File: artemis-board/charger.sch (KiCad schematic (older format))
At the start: 23 parts, among them J10 External NTC, J2 Thermistor, Q2 2N7002, SW2 DNP, U3 LC709203FQH, U4 TP4056, U8 XC6206P332MR

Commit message: added part number for button
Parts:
- SW2: LCSC (none) -> C231329
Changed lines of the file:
@@
 F 2 "Button_Switch_SMD:SW_Push_SPST_NO_Alps_SKRK" H 3200 4500 50  0001 C CNN
 F 3 "~" H 3200 4500 50  0001 C CNN
+F 4 "C231329" H 3200 4500 50  0001 C CNN "LCSC"
 	1    3200 4500
 	1    0    0    -1

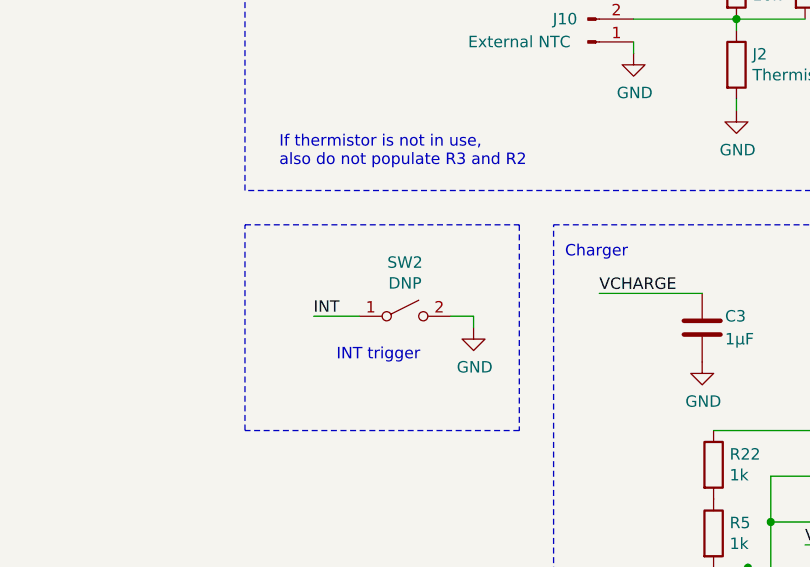
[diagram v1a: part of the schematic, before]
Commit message: changed switch value
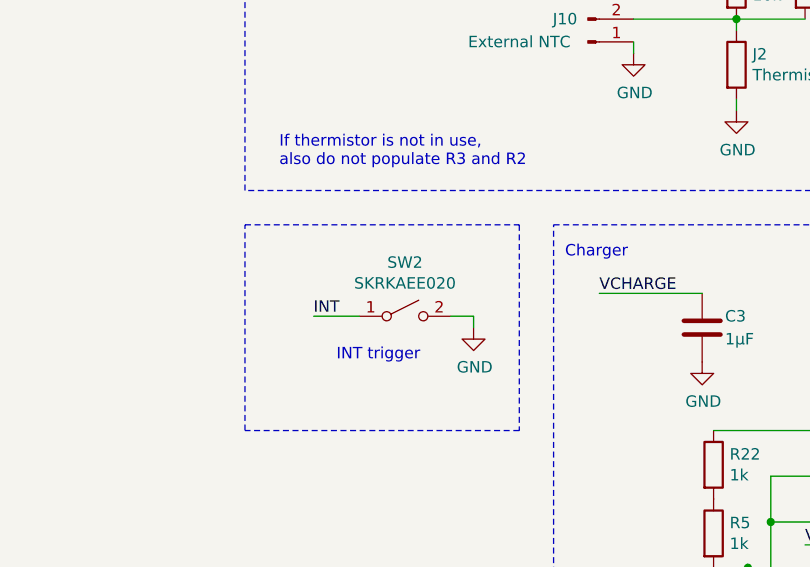
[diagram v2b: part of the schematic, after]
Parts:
- SW2: value DNP -> SKRKAEE020
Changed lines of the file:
@@
 AR Path="/5F639F48/601AEE0F" Ref="SW2"  Part="1"
 F 0 "SW2" H 3200 4735 50  0000 C CNN
-F 1 "DNP" H 3200 4644 50  0000 C CNN
+F 1 "SKRKAEE020" H 3200 4644 50  0000 C CNN
 F 2 "Button_Switch_SMD:SW_Push_SPST_NO_Alps_SKRK" H 3200 4500 50  0001 C CNN
 F 3 "~" H 3200 4500 50  0001 C CNN

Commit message: applied changes to board
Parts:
- removed R5: 1k, Resistor_SMD:R_0603_1608Metric_Pad1.05x0.95mm_HandSolder, symbol Device:R
- R22: value 1k -> 2.4k; LCSC C21190 -> C22940
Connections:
- net GND: now also R22.2
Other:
- moved on the sheet: R22
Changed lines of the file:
@@
 $Comp
 L Device:R R?
-U 1 1 5FD8F02D
+U 1 1 5FD924F7
 P 4550 5450
-AR Path="/5F639CFE/5FD8F02D" Ref="R?"  Part="1"
-AR Path="/5F639F48/5FD8F02D" Ref="R5"  Part="1"
-F 0 "R5" H 4620 5496 50  0000 L CNN
-F 1 "1k" H 4620 5405 50  0000 L CNN
+AR Path="/5F639CFE/5FD924F7" Ref="R?"  Part="1"
+AR Path="/5F639F48/5FD924F7" Ref="R22"  Part="1"
+F 0 "R22" H 4620 5496 50  0000 L CNN
+F 1 "2.4k" H 4620 5405 50  0000 L CNN
 F 2 "Resistor_SMD:R_0603_1608Metric_Pad1.05x0.95mm_HandSolder" V 4480 5450 50  0001 C CNN
 F 3 "~" H 4550 5450 50  0001 C CNN
-F 4 "C21190" H 4550 5450 50  0001 C CNN "LCSC"
+F 4 "C22940" H 4550 5450 50  0001 C CNN "LCSC"
 	1    4550 5450
 	1    0    0    -1
 $EndComp
-$Comp
-L Device:R R?
-U 1 1 5FD924F7
-P 4550 5150
-AR Path="/5F639CFE/5FD924F7" Ref="R?"  Part="1"
-AR Path="/5F639F48/5FD924F7" Ref="R22"  Part="1"
-F 0 "R22" H 4620 5196 50  0000 L CNN
-F 1 "1k" H 4620 5105 50  0000 L CNN
-F 2 "Resistor_SMD:R_0603_1608Metric_Pad1.05x0.95mm_HandSolder" V 4480 5150 50  0001 C CNN
-F 3 "~" H 4550 5150 50  0001 C CNN
-F 4 "C21190" H 4550 5150 50  0001 C CNN "LCSC"
-	1    4550 5150
-	1    0    0    -1
-$EndComp
-Wire Wire Line
-	5300 5300 5250 5300
-Wire Wire Line
-	5250 5300 5250 5000
-Wire Wire Line
-	5250 5000 4550 5000
 $Comp
 L Device:D_Schottky D?
@@
 Text Label 1550 1250 0    50   ~ 0
 3v3_I2C
+Wire Wire Line
+	4550 5300 5300 5300
 $EndSCHEMATC

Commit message: swapped switch for cheaper alps one
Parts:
- SW2: LCSC C231329 -> C115357
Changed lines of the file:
@@
 F 2 "Button_Switch_SMD:SW_Push_SPST_NO_Alps_SKRK" H 3200 4500 50  0001 C CNN
 F 3 "~" H 3200 4500 50  0001 C CNN
-F 4 "C231329" H 3200 4500 50  0001 C CNN "LCSC"
+F 4 "C115357" H 3200 4500 50  0001 C CNN "LCSC"
 	1    3200 4500
 	1    0    0    -1

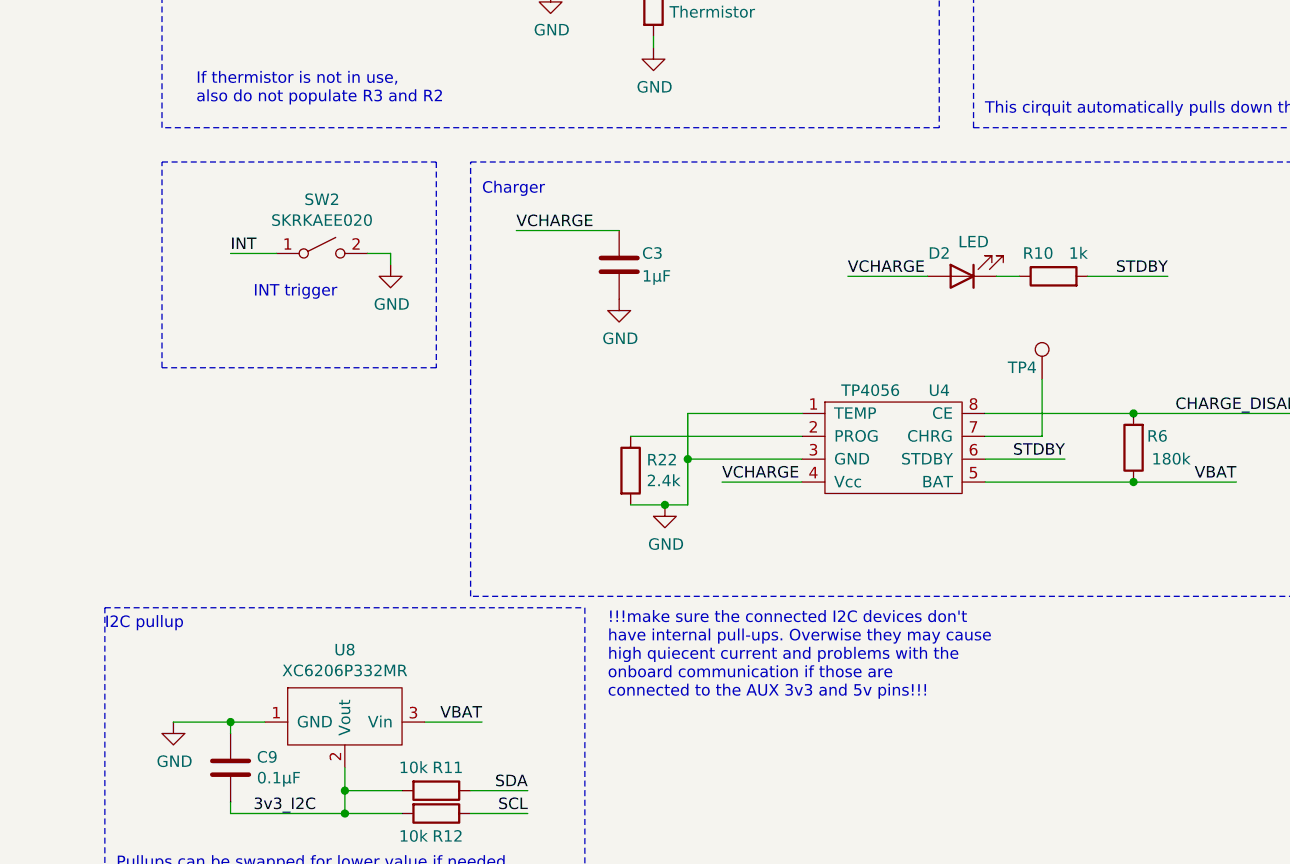
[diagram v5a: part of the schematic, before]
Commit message: added comments and swapped polarity of Vin connector
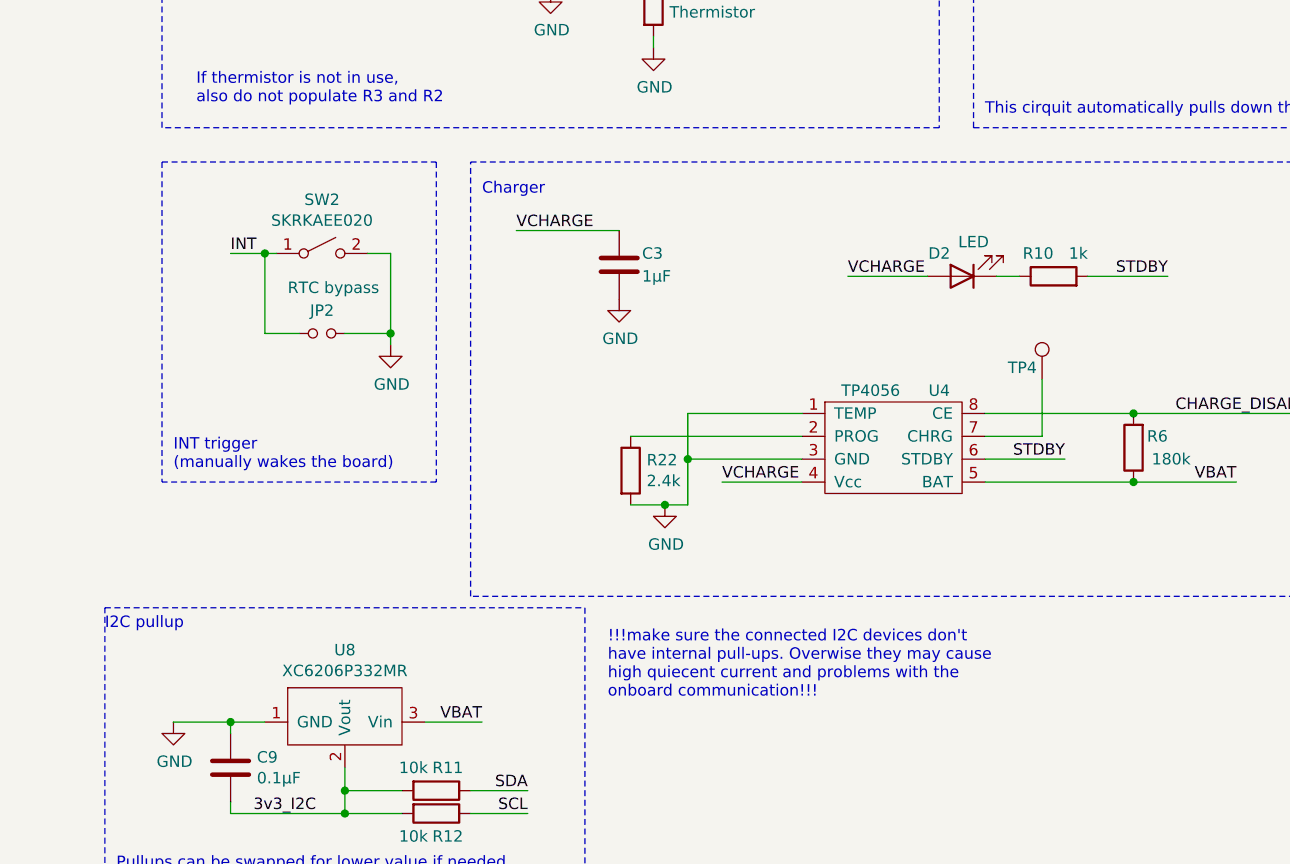
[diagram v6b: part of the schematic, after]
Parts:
- added JP2: RTC bypass, Connector_PinHeader_2.54mm:PinHeader_1x02_P2.54mm_Vertical, symbol Device:Jumper_NO_Small
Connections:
- net GND: now also JP2.1
- net INT: now also JP2.2
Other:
- note added: "!!!make sure the connected I2C devices don't\nhave internal pull-ups. Overwise they may cause\nhigh quiecent current and problems with the\nonboard communication!!!"
- note added: "INT trigger\n(manually wakes the board)"
- note removed: "!!!make sure the connected I2C devices don't\nhave internal pull-ups. Overwise they may cause\nhigh quiecent current and problems with the\nonboard communication if those are\nconnected to the AUX 3v3 and 5v pins!!!"
- note removed: "INT trigger"
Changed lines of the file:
@@
 L power:GND #PWR0133
 U 1 1 601AEE17
-P 3500 4550
-F 0 "#PWR0133" H 3500 4300 50  0001 C CNN
-F 1 "GND" H 3505 4377 50  0000 C CNN
-F 2 "" H 3500 4550 50  0001 C CNN
-F 3 "" H 3500 4550 50  0001 C CNN
-	1    3500 4550
+P 3500 4900
+F 0 "#PWR0133" H 3500 4650 50  0001 C CNN
+F 1 "GND" H 3505 4727 50  0000 C CNN
+F 2 "" H 3500 4900 50  0001 C CNN
+F 3 "" H 3500 4900 50  0001 C CNN
+	1    3500 4900
 	1    0    0    -1
 $EndComp
-Wire Wire Line
-	3500 4550 3500 4500
 Wire Wire Line
 	3400 4500 3500 4500
@@
 INT
 Wire Wire Line
-	3000 4500 2800 4500
-Text Notes 2900 4700 0    50   ~ 0
-INT trigger
+	3000 4500 2950 4500
+Text Notes 2550 5450 0    50   ~ 0
+INT trigger\n(manually wakes the board)
 Wire Notes Line
 	2500 4100 3700 4100
 Wire Notes Line
-	3700 4100 3700 5000
-Wire Notes Line
-	3700 5000 2500 5000
-Wire Notes Line
-	2500 5000 2500 4100
+	3700 5500 2500 5500
 Wire Notes Line
 	2350 600  2350 2100
@@
 Pullups can be swapped for lower value if needed
 Text Notes 4450 6450 0    50   ~ 0
-!!!make sure the connected I2C devices don't\nhave internal pull-ups. Overwise they may cause\nhigh quiecent current and problems with the\nonboard communication if those are\nconnected to the AUX 3v3 and 5v pins!!!
+!!!make sure the connected I2C devices don't\nhave internal pull-ups. Overwise they may cause\nhigh quiecent current and problems with the\nonboard communication!!!
 Text Label 2900 6950 0    50   ~ 0
 3v3_I2C
@@
 Wire Wire Line
 	4550 5300 5300 5300
+$Comp
+L Device:Jumper_NO_Small JP?
+U 1 1 60B74E13
+P 3200 4850
+AR Path="/5F63A0E9/60B74E13" Ref="JP?"  Part="1"
+AR Path="/5F639F48/60B74E13" Ref="JP2"  Part="1"
+F 0 "JP2" H 3200 4750 50  0000 C CNN
+F 1 "RTC bypass" H 3150 4650 50  0000 C CNN
+F 2 "Connector_PinHeader_2.54mm:PinHeader_1x02_P2.54mm_Vertical" H 3200 4850 50  0001 C CNN
+F 3 "~" H 3200 4850 50  0001 C CNN
+	1    3200 4850
+	-1   0    0    1
+$EndComp
+Wire Notes Line
+	3700 4100 3700 5500
+Wire Wire Line
+	3500 4850 3500 4900
+Wire Wire Line
+	3300 4850 3500 4850
+Wire Wire Line
+	3500 4500 3500 4850
+Connection ~ 3500 4850
+Wire Wire Line
+	3100 4850 2950 4850
+Wire Wire Line
+	2950 4850 2950 4500
+Connection ~ 2950 4500
+Wire Wire Line
+	2950 4500 2800 4500
+Wire Notes Line
+	2500 4100 2500 5500
 $EndSCHEMATC

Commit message: added 1µ cap close to 3v3 I2C regulator
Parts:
- added C27: 1µF, Capacitor_SMD:C_0603_1608Metric_Pad1.08x0.95mm_HandSolder, symbol Device:C
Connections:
- net GND: now also C27.2
- net VBAT: now also C27.1
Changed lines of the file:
@@
 SDA
 Wire Wire Line
-	2800 6550 2550 6550
+	2800 6550 2700 6550
 $Comp
 L power:GND #PWR?
@@
 Wire Notes Line
 	2500 4100 2500 5500
+$Comp
+L Device:C C27
+U 1 1 60B69250
+P 2700 6400
+F 0 "C27" H 2800 6450 50  0000 L CNN
+F 1 "1µF" H 2800 6350 50  0000 L CNN
+F 2 "Capacitor_SMD:C_0603_1608Metric_Pad1.08x0.95mm_HandSolder" H 2738 6250 50  0001 C CNN
+F 3 "~" H 2700 6400 50  0001 C CNN
+F 4 "C15849" H 2700 6400 50  0001 C CNN "LCSC"
+	1    2700 6400
+	1    0    0    -1
+$EndComp
+Connection ~ 2700 6550
+Wire Wire Line
+	2700 6550 2550 6550
+Wire Wire Line
+	2700 6250 2950 6250
+Text Label 2950 6250 2    50   ~ 0
+VBAT
 $EndSCHEMATC

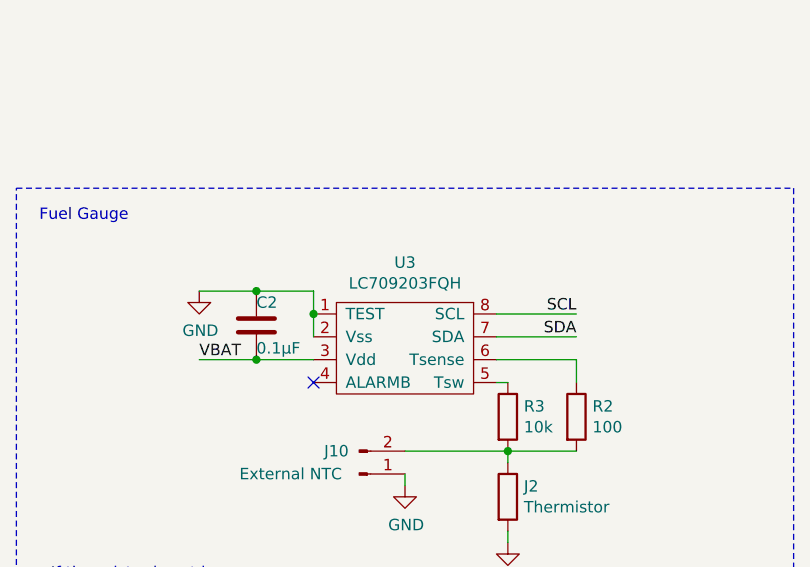
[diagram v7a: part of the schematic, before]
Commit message: swapped and added some lcsc part numbers and DNP markers
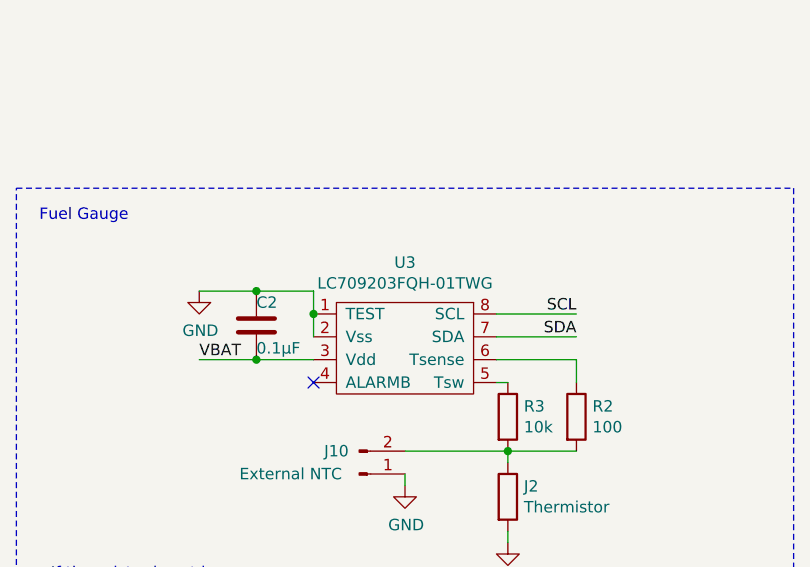
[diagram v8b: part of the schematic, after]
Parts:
- C3, C4: footprint Capacitor_SMD:C_0603_1608Metric_Pad1.05x0.95mm_HandSolder -> Capacitor_SMD:C_0603_1608Metric_Pad1.08x0.95mm_HandSolder
- D3: LCSC C8598 -> C8598
- J10, JP2: DNP (none) -> DNP
- U3: value LC709203FQH -> LC709203FQH-01TWG
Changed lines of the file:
@@
 F 0 "C4" H 7350 2850 50  0000 L CNN
 F 1 "1µF" H 7350 2750 50  0000 L CNN
-F 2 "Capacitor_SMD:C_0603_1608Metric_Pad1.05x0.95mm_HandSolder" H 7288 2650 50  0001 C CNN
+F 2 "Capacitor_SMD:C_0603_1608Metric_Pad1.08x0.95mm_HandSolder" H 7288 2650 50  0001 C CNN
 F 3 "~" H 7250 2800 50  0001 C CNN
 F 4 "C15849" H 7250 2800 50  0001 C CNN "LCSC"
@@
 F 0 "C3" H 4600 4600 50  0000 L CNN
 F 1 "1µF" H 4600 4500 50  0000 L CNN
-F 2 "Capacitor_SMD:C_0603_1608Metric_Pad1.05x0.95mm_HandSolder" H 4538 4400 50  0001 C CNN
+F 2 "Capacitor_SMD:C_0603_1608Metric_Pad1.08x0.95mm_HandSolder" H 4538 4400 50  0001 C CNN
 F 3 "~" H 4500 4550 50  0001 C CNN
 F 4 "C15849" H 4500 4550 50  0001 C CNN "LCSC"
@@
 P 4200 2750
 F 0 "U3" H 4200 3125 50  0000 C CNN
-F 1 "LC709203FQH" H 4200 3034 50  0000 C CNN
+F 1 "LC709203FQH-01TWG" H 4200 3034 50  0000 C CNN
 F 2 "Package_DFN_QFN:WDFN-8-1EP_4x3mm_P0.65mm_EP2.4x1.8mm" H 4250 2500 50  0001 C CNN
 F 3 "https://www.onsemi.com/pub/Collateral/LC709203F-D.PDF" H 4200 2800 50  0001 C CNN
@@
 F 2 "Diode_SMD:D_SOD-123" H 7100 3200 50  0001 C CNN
 F 3 "https://datasheet.lcsc.com/szlcsc/Changjiang-Electronics-Tech-CJ-B5819W_C8598.pdf" H 7100 3200 50  0001 C CNN
-F 4 " C8598" H 7100 3200 50  0001 C CNN "LCSC"
+F 4 "C8598" H 7100 3200 50  0001 C CNN "LCSC"
 	1    7100 3200
 	0    1    1    0
@@
 F 3 "" H 4000 3300 50  0001 C CNN
 F 4 "" H 4000 3300 50  0001 C CNN "LCSC"
+F 5 "DNP" H 4000 3300 50  0001 C CNN "DNP"
 	1    4000 3300
 	1    0    0    1
@@
 F 2 "Connector_PinHeader_2.54mm:PinHeader_1x02_P2.54mm_Vertical" H 3200 4850 50  0001 C CNN
 F 3 "~" H 3200 4850 50  0001 C CNN
+F 4 "DNP" H 3200 4850 50  0001 C CNN "DNP"
 	1    3200 4850
 	-1   0    0    1
